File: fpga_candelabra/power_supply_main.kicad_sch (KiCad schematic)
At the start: 22 parts, among them U7 TPS54821, U9 HT7533-1

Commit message: fpga_candelabra: add ddr4 power and sysmon mcu periph, bump library
Signed-off-by: Yichuan Gao <gaoyichuan000@gmail.com>
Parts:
- removed U9: HT7533-1, Package_TO_SOT_SMD:SOT-89-3, symbol Regulator_Linear:HT75xx-1-SOT89
- added C170: 22uF 25V, Capacitor_SMD:C_1206_3216Metric, symbol Device:C_Small
- added U9: AMS1117-3.3, Package_TO_SOT_SMD:SOT-223-3_TabPin2, symbol Regulator_Linear:AMS1117-3.3
- C67, C68: value 4.7uF -> 22uF 25V; footprint Capacitor_SMD:C_0402_1005Metric -> Capacitor_SMD:C_1206_3216Metric
- C70: value 100uF 10V -> 22uF 25V
- C72: value 1uF -> 4.7uF 10V
- C73: value 1uF -> 22uF 25V; footprint Capacitor_SMD:C_0402_1005Metric -> Capacitor_SMD:C_1206_3216Metric
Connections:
- net +12V: now also U9.3 (VI)
- net +3.3VAUX: now also U9.2 (VO)
- net +5V: now also C170.1
- net Earth: now also C170.2, U9.1 (GND)
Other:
- note added: "5V Main -> 3.3V 500mA Aux (Always on, for SYSMON MCU)"
- note removed: "12V Input -> 3.3V 50mA Aux (Always on, for SYSMON MCU)"
- moved on the sheet: C71

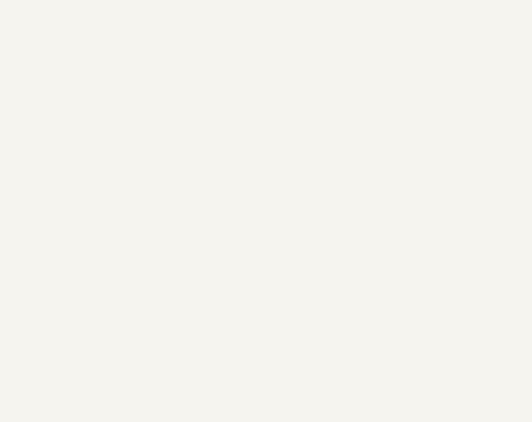
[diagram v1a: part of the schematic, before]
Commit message: fpga_candelabra: add clock pll, refactor fmc power
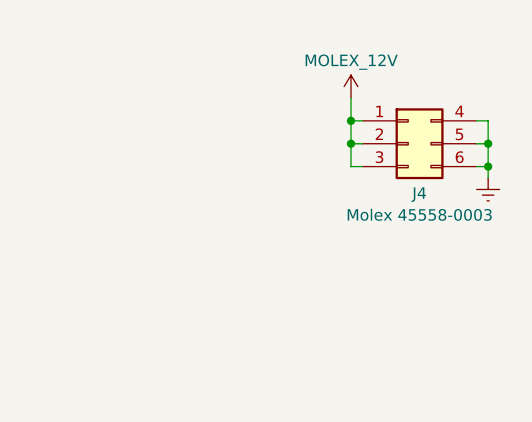
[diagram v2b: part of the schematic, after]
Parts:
- added J4: Molex 45558-0003, Connector_Molex:Molex_Mini-Fit_Jr_5569-06A2_2x03_P4.20mm_Horizontal, symbol Connector_Generic:Conn_02x03_Top_Bottom
- U7: footprint Package_DFN_QFN:Texas_VQFN-RHL-20 -> CHIPSAlliance_Package_DFN_QFN:Texas_VQFN-RHL-14
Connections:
- net Earth: now also J4.4 (Pin_4), J4.5 (Pin_5), J4.6 (Pin_6)
- new net MOLEX_12V: J4.1 (Pin_1), J4.2 (Pin_2), J4.3 (Pin_3)

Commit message: fpga_candelabra: major revision
* Finish DDR4 & QSFP+ & PCIe layout
* Change FMC to LPC
* Add mikroBUS extension
* 12V input & PDN updates
* FPGA config updates

Signed-off-by: Yichuan Gao <gaoyichuan000@gmail.com>
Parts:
- added C322, C323, C324, C325, C326: 100nF, Capacitor_SMD:C_0402_1005Metric, symbol Device:C_Small
- added J9: Molex 45586-0005, CHIPSAlliance_Connector:Molex_Mini-Fit_Jr_45586-0005_2x04_P4.20mm_Horizontal, symbol Connector_Generic:Conn_02x04_Top_Bottom
- added Q4, Q5, Q6, Q7, Q8: AON7544, CHIPSAlliance_Package_DFN_QFN:AO_DFN3x3A_8L_EP1_P_DFN-10-1EP_3x3mm_P0.65mm_EP1.98x2.45mm, symbol CHIPSAlliance_Transistor_FET:AON7544
- added R146, R147, R148, R149, R150: 100R, Resistor_SMD:R_0402_1005Metric, symbol Device:R_Small
- added U25, U26, U27, U28, U29: LM5050-1, Package_TO_SOT_SMD:TSOT-23-6, symbol Power_Management:LM5050-1
- J4: value Molex 45558-0003 -> Molex 45558-0002; footprint Connector_Molex:Molex_Mini-Fit_Jr_5569-06A2_2x03_P4.20mm_Horizontal -> CHIPSAlliance_Connector:Molex_Mini-Fit_Jr_45558-0003_2x03_P4.20mm_Horizontal
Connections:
- net +3.3VAUX: now also C72.1; no longer C73.1
- net Earth: now also C322.2, C323.2, C324.2, C325.2, C326.2, J9.4 (Pin_4), J9.5 (Pin_5), J9.6 (Pin_6), J9.7 (Pin_7), J9.8 (Pin_8), U25.2 (GND), U25.3 (OFF), U26.2 (GND), U26.3 (OFF), U27.2 (GND), U27.3 (OFF), U28.2 (GND), U28.3 (OFF), U29.2 (GND), U29.3 (OFF)
- net +12V renamed +12V_G2
- net +12V_G2: now also Q5.5 (D), Q7.1 (S), Q7.2 (S), Q7.3 (S), Q8.1 (S), Q8.2 (S), Q8.3 (S), R147.2, U26.6 (OUT), U28.4 (IN), U29.4 (IN); no longer C72.1, U9.3 (VI)
- net MOLEX_12V renamed MOLEX_6P_12V
- net MOLEX_6P_12V: now also Q5.1 (S), Q5.2 (S), Q5.3 (S), U26.4 (IN)
- new net: C325.1, R149.1, U28.1 (VS)
- new net: Q7.4 (G), U28.5 (GATE)
- new net: C326.1, R150.1, U29.1 (VS)
- new net: C323.1, R147.1, U26.1 (VS)
- new net: C324.1, R148.1, U27.1 (VS)
- new net: Q5.4 (G), U26.5 (GATE)
- new net: Q6.4 (G), U27.5 (GATE)
- new net: C322.1, R146.1, U25.1 (VS)
- new net: Q8.4 (G), U29.5 (GATE)
- new net: Q4.4 (G), U25.5 (GATE)
- new net +12V_G1: Q4.5 (D), Q7.5 (D), R146.2, R149.2, U25.6 (OUT), U28.6 (OUT)
- new net +12V_G3: C73.1, Q6.5 (D), Q8.5 (D), R148.2, R150.2, U27.6 (OUT), U29.6 (OUT), U9.3 (VI)
- new net MOLEX_8P_12V: J9.1 (Pin_1), J9.2 (Pin_2), J9.3 (Pin_3), Q4.1 (S), Q4.2 (S), Q4.3 (S), U25.4 (IN)
- new net PCIE_12V_IN: Q6.1 (S), Q6.2 (S), Q6.3 (S), U27.4 (IN)
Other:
- moved on the sheet: C72, C73, J4

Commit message: fpga_candelabra: sch & layout v0.5, pass basic ERC & DRC
Signed-off-by: Yichuan Gao <gaoyichuan000@gmail.com>
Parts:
- added C349: 47uF 6.3V, Capacitor_SMD:C_0603_1608Metric, symbol Device:C_Small
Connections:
- net +3.3VAUX: now also C349.1
- net Earth: now also C349.2

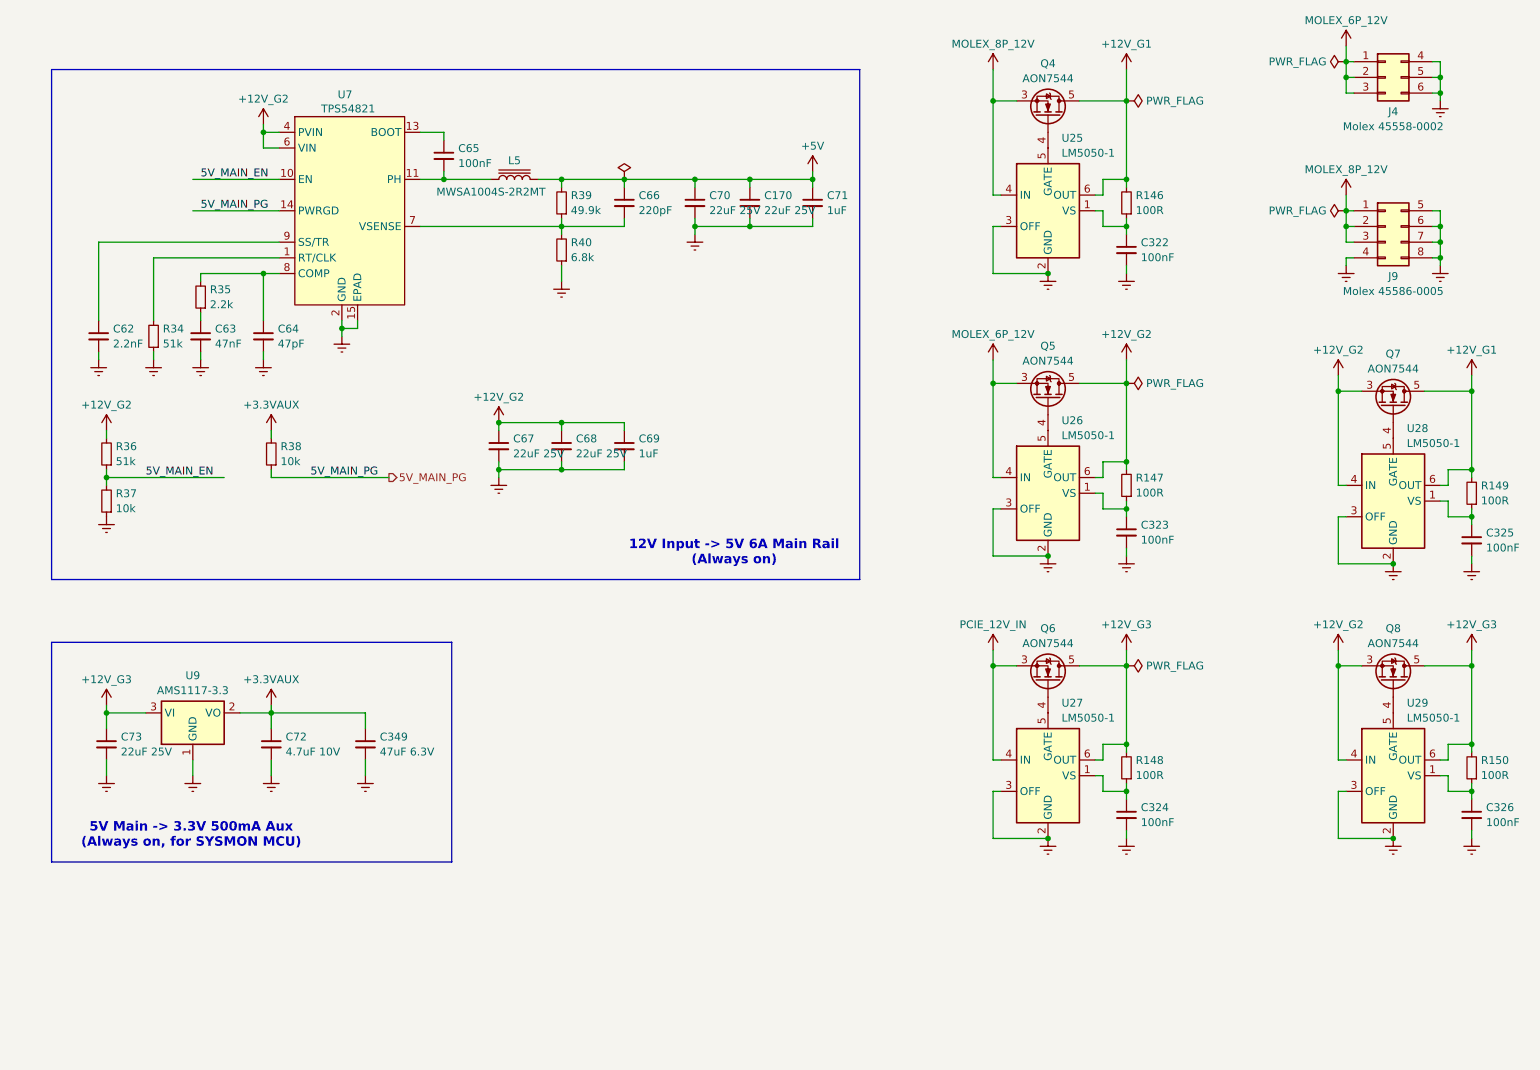
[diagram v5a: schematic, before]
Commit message: fpga_candelabra: first rev fixes - fix vccint power stage FCCM mode - add ddr4 vref decoupling cap - refactor status LEDs - minor layout changes
Signed-off-by: Yichuan Gao <gaoyichuan000@gmail.com>
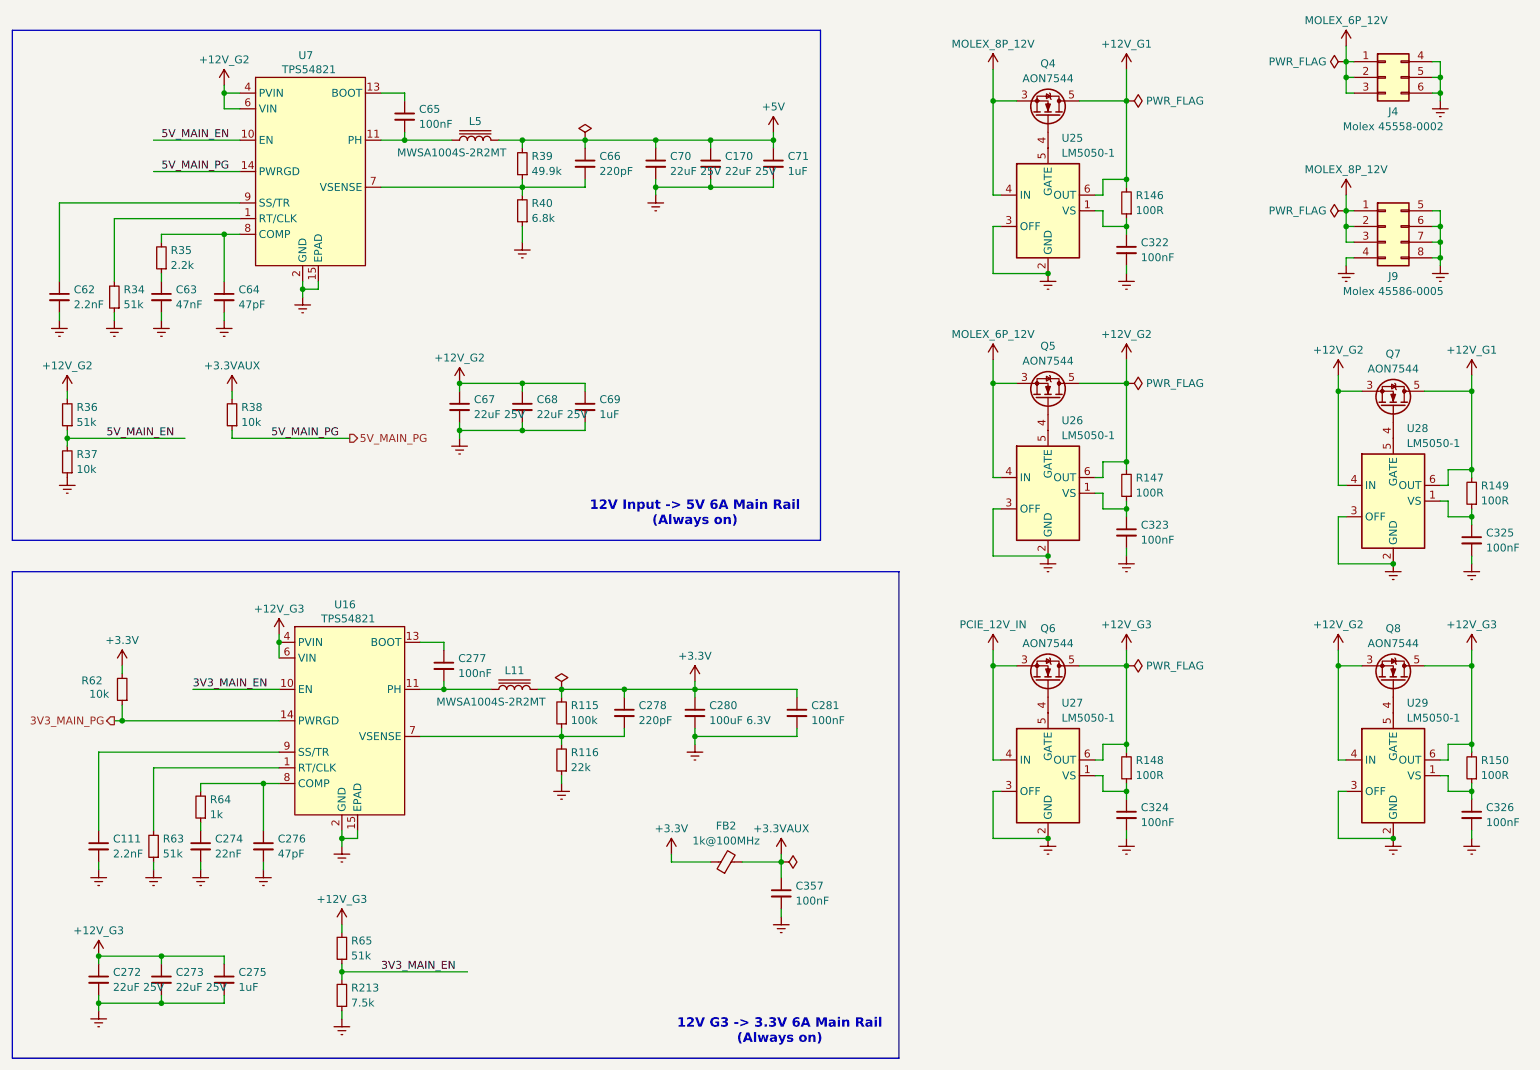
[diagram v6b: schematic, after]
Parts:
- removed C349: 47uF 6.3V, Capacitor_SMD:C_0603_1608Metric, symbol Device:C_Small
- removed C72: 4.7uF 10V, Capacitor_SMD:C_0402_1005Metric, symbol Device:C_Small
- removed C73: 22uF 25V, Capacitor_SMD:C_1206_3216Metric, symbol Device:C_Small
- removed U9: AMS1117-3.3, Package_TO_SOT_SMD:SOT-223-3_TabPin2, symbol Regulator_Linear:AMS1117-3.3
- added C111: 2.2nF, Capacitor_SMD:C_0402_1005Metric, symbol Device:C_Small
- added C272, C273: 22uF 25V, Capacitor_SMD:C_1206_3216Metric, symbol Device:C_Small
- added C274: 22nF, Capacitor_SMD:C_0402_1005Metric, symbol Device:C_Small
- added C275: 1uF, Capacitor_SMD:C_0402_1005Metric, symbol Device:C_Small
- added C276: 47pF, Capacitor_SMD:C_0402_1005Metric, symbol Device:C_Small
- added C277, C281, C357: 100nF, Capacitor_SMD:C_0402_1005Metric, symbol Device:C_Small
- added C278: 220pF, Capacitor_SMD:C_0402_1005Metric, symbol Device:C_Small
- added C280: 100uF 6.3V, Capacitor_SMD:C_1206_3216Metric, symbol Device:C_Small
- added FB2: 1k@100MHz, Inductor_SMD:L_0402_1005Metric, symbol Device:FerriteBead_Small
- added L11: MWSA1004S-2R2MT, Inductor_SMD:L_Sunlord_MWSA1004S, symbol Device:L_Iron
- added R115: 100k, Resistor_SMD:R_0402_1005Metric, symbol Device:R_Small
- added R116: 22k, Resistor_SMD:R_0402_1005Metric, symbol Device:R_Small
- added R213: 7.5k, Resistor_SMD:R_0402_1005Metric, symbol Device:R_Small
- added R62: 10k, Resistor_SMD:R_0402_1005Metric, symbol Device:R_Small
- added R63, R65: 51k, Resistor_SMD:R_0402_1005Metric, symbol Device:R_Small
- added R64: 1k, Resistor_SMD:R_0402_1005Metric, symbol Device:R_Small
- added U16: TPS54821, CHIPSAlliance_Package_DFN_QFN:Texas_VQFN-RHL-14, symbol CHIPSAlliance_Regulator_Switching:TPS54821
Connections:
- net +12V_G3: now also C272.1, C273.1, C275.1, R65.2, U16.4 (PVIN), U16.5 (PVIN), U16.6 (VIN)
- net +3.3VAUX: now also C357.1, FB2.2
- net Earth: now also C111.2, C272.2, C273.2, C274.2, C275.2, C276.2, C280.2, C281.2, C357.2, R116.1, R213.1, R63.1, U16.15 (EPAD), U16.2 (GND), U16.3 (GND)
- new net: C277.2, L11.1, U16.11 (PH), U16.12 (PH)
- new net: C274.1, R64.1
- new net: C276.1, R64.2, U16.8 (COMP)
- new net: C111.1, U16.9 (SS/TR)
- new net: R63.2, U16.1 (RT/CLK)
- new net: C277.1, U16.13 (BOOT)
- new net: C278.2, R115.1, R116.2, U16.7 (VSENSE)
- new net +3.3V: C278.1, C280.1, C281.1, FB2.1, L11.2, R115.2, R62.2
- new net 3V3_MAIN_EN: R213.2, R65.1, U16.10 (EN)
- new net 3V3_MAIN_PG: R62.1, U16.14 (PWRGD)
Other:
- note added: "12V G3 -> 3.3V 6A Main Rail (Always on)"
- note removed: "5V Main -> 3.3V 500mA Aux (Always on, for SYSMON MCU)"
- moved on the sheet: C170, C62, C63, C64, C65, C66, C67, C68, C69, C70, C71, L5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

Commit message: fpga_candelabra: add author & rev to schematics
Signed-off-by: Yichuan Gao <gaoyichuan000@gmail.com>
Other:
- company: (none) -> CHIPS Alliance
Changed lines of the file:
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@@
 	(title_block
 		(title "Power Supply 1 (Main 5V, Aux 3.3V)")
+		(date "2025-02-05")
+		(rev "0.2.0")
+		(company "CHIPS Alliance")
+		(comment 1 "Yichuan Gao")
+		(comment 2 "Yichuan Gao")
 	)
 	(junction
